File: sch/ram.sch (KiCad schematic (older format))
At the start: 49 parts

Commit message: Start to move to a bit more affordable components
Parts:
- R24, R39, R40, R41, R42, R43, R44, R45, R46, R7, R77, R78, R79, R8, R80, R9: value 51 -> RES
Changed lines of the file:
@@
 EESchema Schematic File Version 2
+LIBS:aleste-rescue
 LIBS:mylib
 LIBS:power
@@
 encoding utf-8
 Sheet 2 7
-Title "Aleste 520EX"
+Title "Aleste 520M"
 Date "1994-01-04"
 Rev ""
-Comp "Patisonic"
-Comment1 "Restored by Alexander Molodtsov"
-Comment2 "Aleste 520EX"
+Comp "Alexander Molodtsov"
+Comment1 ""
+Comment2 ""
 Comment3 ""
 Comment4 ""
@@
 P 10300 1600
 F 0 "R39" H 10300 1700 50  0000 C CNN
-F 1 "51" H 10300 1500 50  0000 C CNN
+F 1 "RES" H 10300 1500 50  0000 C CNN
 F 2 "MyLib:Resistor_Horizontal_RM7.5mm" H 10300 1550 60  0001 C CNN
 F 3 "" H 10300 1550 60  0000 C CNN
@@
 P 10300 2500
 F 0 "R40" H 10300 2600 50  0000 C CNN
-F 1 "51" H 10300 2400 50  0000 C CNN
+F 1 "RES" H 10300 2400 50  0000 C CNN
 F 2 "MyLib:Resistor_Horizontal_RM7.5mm" H 10300 2450 60  0001 C CNN
 F 3 "" H 10300 2450 60  0000 C CNN
@@
 P 10300 3500
 F 0 "R41" H 10300 3600 50  0000 C CNN
-F 1 "51" H 10300 3400 50  0000 C CNN
+F 1 "RES" H 10300 3400 50  0000 C CNN
 F 2 "MyLib:Resistor_Horizontal_RM7.5mm" H 10300 3450 60  0001 C CNN
 F 3 "" H 10300 3450 60  0000 C CNN
@@
 P 10300 4400
 F 0 "R42" H 10300 4500 50  0000 C CNN
-F 1 "51" H 10300 4300 50  0000 C CNN
+F 1 "RES" H 10300 4300 50  0000 C CNN
 F 2 "MyLib:Resistor_Horizontal_RM7.5mm" H 10300 4350 60  0001 C CNN
 F 3 "" H 10300 4350 60  0000 C CNN
@@
 P 10300 5400
 F 0 "R43" H 10300 5500 50  0000 C CNN
-F 1 "51" H 10300 5300 50  0000 C CNN
+F 1 "RES" H 10300 5300 50  0000 C CNN
 F 2 "MyLib:Resistor_Horizontal_RM7.5mm" H 10300 5350 60  0001 C CNN
 F 3 "" H 10300 5350 60  0000 C CNN
@@
 P 10300 6300
 F 0 "R44" H 10300 6400 50  0000 C CNN
-F 1 "51" H 10300 6200 50  0000 C CNN
+F 1 "RES" H 10300 6200 50  0000 C CNN
 F 2 "MyLib:Resistor_Horizontal_RM7.5mm" H 10300 6250 60  0001 C CNN
 F 3 "" H 10300 6250 60  0000 C CNN
@@
 P 10300 7300
 F 0 "R45" H 10300 7400 50  0000 C CNN
-F 1 "51" H 10300 7200 50  0000 C CNN
+F 1 "RES" H 10300 7200 50  0000 C CNN
 F 2 "MyLib:Resistor_Horizontal_RM7.5mm" H 10300 7250 60  0001 C CNN
 F 3 "" H 10300 7250 60  0000 C CNN
@@
 P 10300 8200
 F 0 "R46" H 10300 8300 50  0000 C CNN
-F 1 "51" H 10300 8100 50  0000 C CNN
+F 1 "RES" H 10300 8100 50  0000 C CNN
 F 2 "MyLib:Resistor_Horizontal_RM7.5mm" H 10300 8150 60  0001 C CNN
 F 3 "" H 10300 8150 60  0000 C CNN
@@
 P 10300 9000
 F 0 "R24" H 10300 9100 50  0000 C CNN
-F 1 "51" H 10300 8900 50  0000 C CNN
+F 1 "RES" H 10300 8900 50  0000 C CNN
 F 2 "MyLib:Resistor_Horizontal_RM7.5mm" H 10300 8950 60  0001 C CNN
 F 3 "" H 10300 8950 60  0000 C CNN
@@
 P 3100 9700
 F 0 "R7" H 3100 9800 50  0000 C CNN
-F 1 "51" H 3100 9600 50  0000 C CNN
+F 1 "RES" H 3100 9600 50  0000 C CNN
 F 2 "MyLib:Resistor_Horizontal_RM7.5mm" H 3100 9650 60  0001 C CNN
 F 3 "" H 3100 9650 60  0000 C CNN
@@
 P 3500 10400
 F 0 "R9" H 3500 10500 50  0000 C CNN
-F 1 "51" H 3500 10300 50  0000 C CNN
+F 1 "RES" H 3500 10300 50  0000 C CNN
 F 2 "MyLib:Resistor_Horizontal_RM7.5mm" H 3500 10350 60  0001 C CNN
 F 3 "" H 3500 10350 60  0000 C CNN
@@
 P 3500 10900
 F 0 "R8" H 3500 11000 50  0000 C CNN
-F 1 "51" H 3500 10800 50  0000 C CNN
+F 1 "RES" H 3500 10800 50  0000 C CNN
 F 2 "MyLib:Resistor_Horizontal_RM7.5mm" H 3500 10850 60  0001 C CNN
 F 3 "" H 3500 10850 60  0000 C CNN
@@
 P 3000 13800
 F 0 "R77" H 3000 13900 50  0000 C CNN
-F 1 "51" H 3000 13700 50  0000 C CNN
+F 1 "RES" H 3000 13700 50  0000 C CNN
 F 2 "MyLib:Resistor_Horizontal_RM7.5mm" H 3000 13750 60  0001 C CNN
 F 3 "" H 3000 13750 60  0000 C CNN
@@
 P 3400 14000
 F 0 "R78" H 3400 14100 50  0000 C CNN
-F 1 "51" H 3400 13900 50  0000 C CNN
+F 1 "RES" H 3400 13900 50  0000 C CNN
 F 2 "MyLib:Resistor_Horizontal_RM7.5mm" H 3400 13950 60  0001 C CNN
 F 3 "" H 3400 13950 60  0000 C CNN
@@
 P 3000 14200
 F 0 "R79" H 3000 14300 50  0000 C CNN
-F 1 "51" H 3000 14100 50  0000 C CNN
+F 1 "RES" H 3000 14100 50  0000 C CNN
 F 2 "MyLib:Resistor_Horizontal_RM7.5mm" H 3000 14150 60  0001 C CNN
 F 3 "" H 3000 14150 60  0000 C CNN
@@
 P 3400 14400
 F 0 "R80" H 3400 14500 50  0000 C CNN
-F 1 "51" H 3400 14300 50  0000 C CNN
+F 1 "RES" H 3400 14300 50  0000 C CNN
 F 2 "MyLib:Resistor_Horizontal_RM7.5mm" H 3400 14350 60  0001 C CNN
 F 3 "" H 3400 14350 60  0000 C CNN

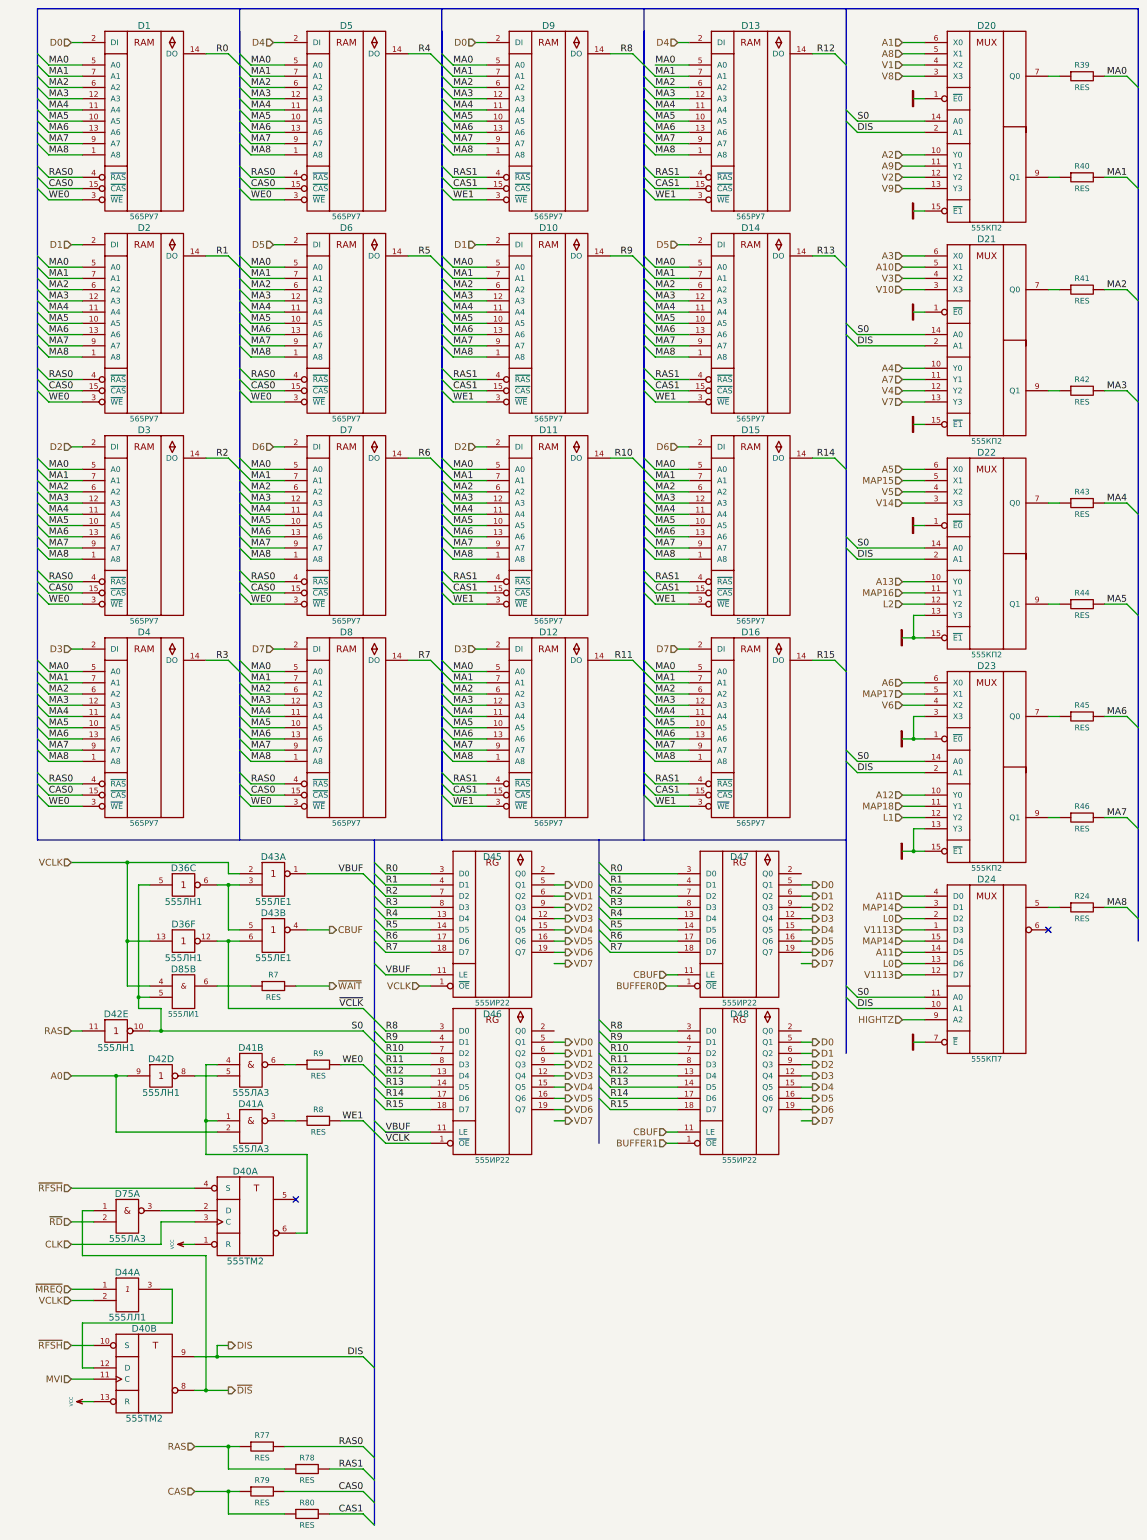
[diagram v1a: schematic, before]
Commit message: Update IR22 and IR23 symbols
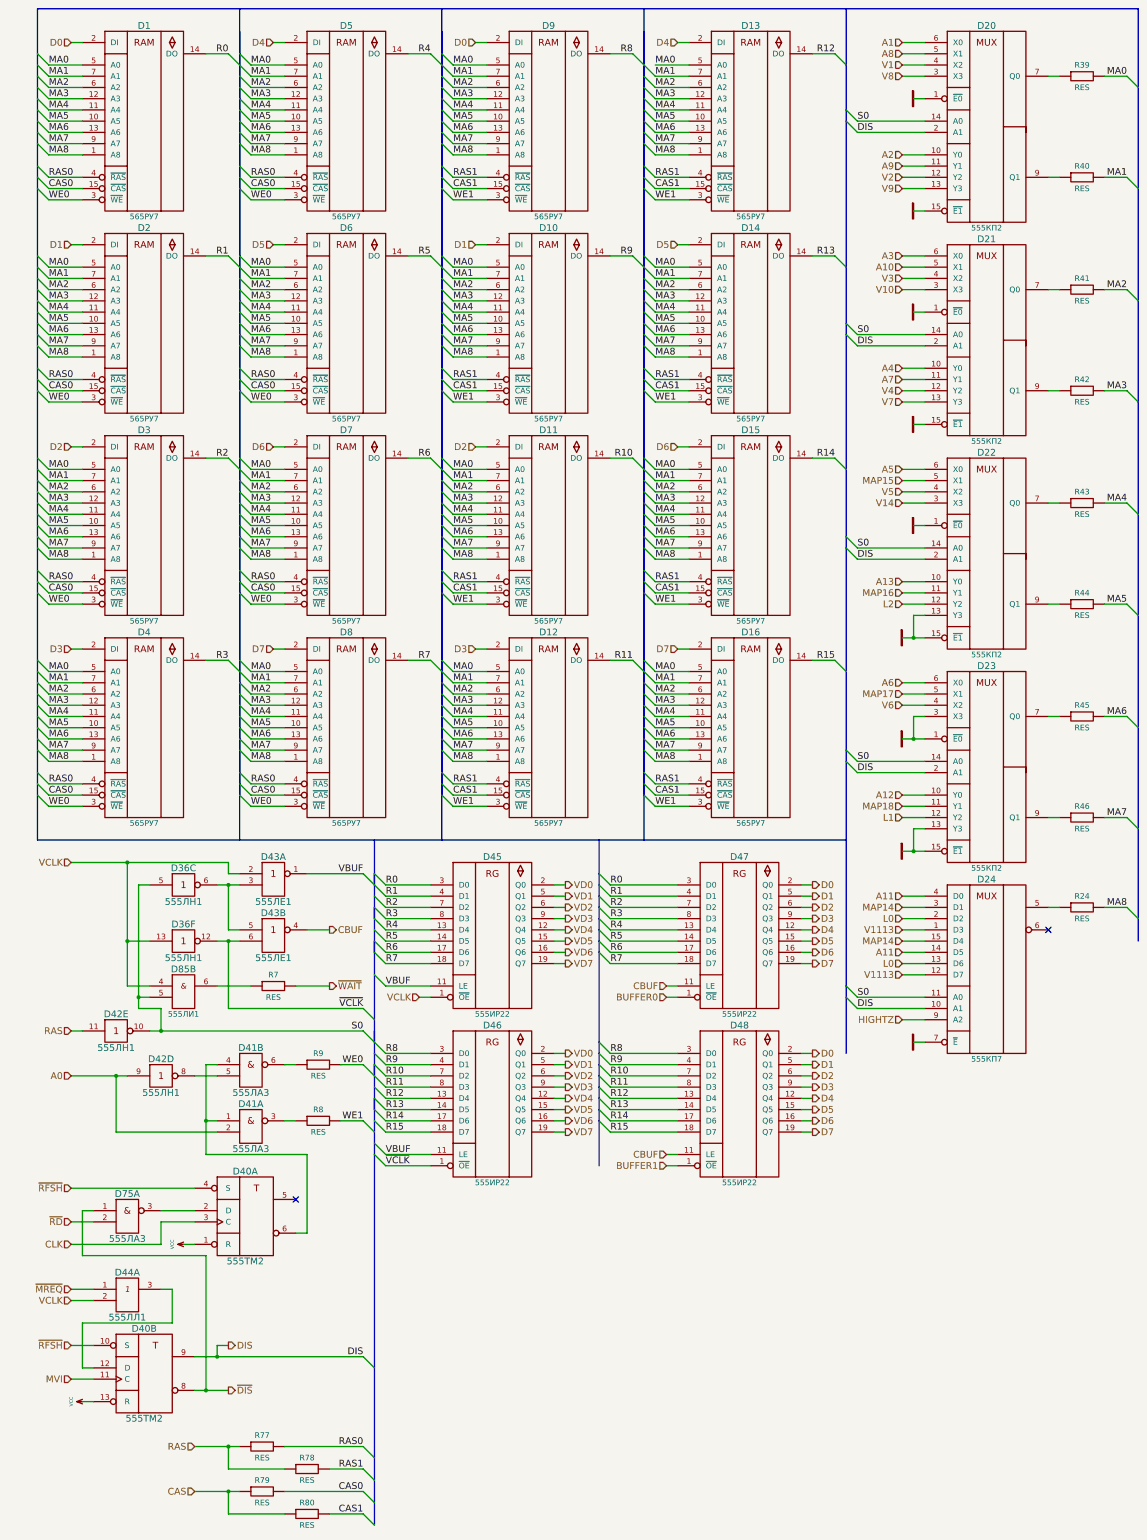
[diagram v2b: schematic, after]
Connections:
- net D0: now also D47.2 (Q0), D48.2 (Q0); no longer D47.5 (Q1), D48.5 (Q1)
- net D1: now also D47.5 (Q1), D48.5 (Q1); no longer D47.6 (Q2), D48.6 (Q2)
- net D2: now also D47.6 (Q2), D48.6 (Q2); no longer D47.9 (Q3), D48.9 (Q3)
- net D3: now also D47.9 (Q3), D48.9 (Q3); no longer D47.12 (Q4), D48.12 (Q4)
- net D4: now also D47.12 (Q4), D48.12 (Q4); no longer D47.15 (Q5), D48.15 (Q5)
- net D5: now also D47.15 (Q5), D48.15 (Q5); no longer D47.16 (Q6), D48.16 (Q6)
- net D6: now also D47.16 (Q6), D48.16 (Q6); no longer D47.19 (Q7), D48.19 (Q7)
- net D7: now also D47.19 (Q7), D48.19 (Q7)
- net VD0: now also D45.2 (Q0), D46.2 (Q0); no longer D45.5 (Q1), D46.5 (Q1)
- net VD1: now also D45.5 (Q1), D46.5 (Q1); no longer D45.6 (Q2), D46.6 (Q2)
- net VD2: now also D45.6 (Q2), D46.6 (Q2); no longer D45.9 (Q3), D46.9 (Q3)
- net VD3: now also D45.9 (Q3), D46.9 (Q3); no longer D45.12 (Q4), D46.12 (Q4)
- net VD4: now also D45.12 (Q4), D46.12 (Q4); no longer D45.15 (Q5), D46.15 (Q5)
- net VD5: now also D45.15 (Q5), D46.15 (Q5); no longer D45.16 (Q6), D46.16 (Q6)
- net VD6: now also D45.16 (Q6), D46.16 (Q6); no longer D45.19 (Q7), D46.19 (Q7)
- net VD7: now also D45.19 (Q7), D46.19 (Q7)
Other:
- moved on the sheet: D45, D46, D47, D48

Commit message: Another ROM replaced with PLD, source included
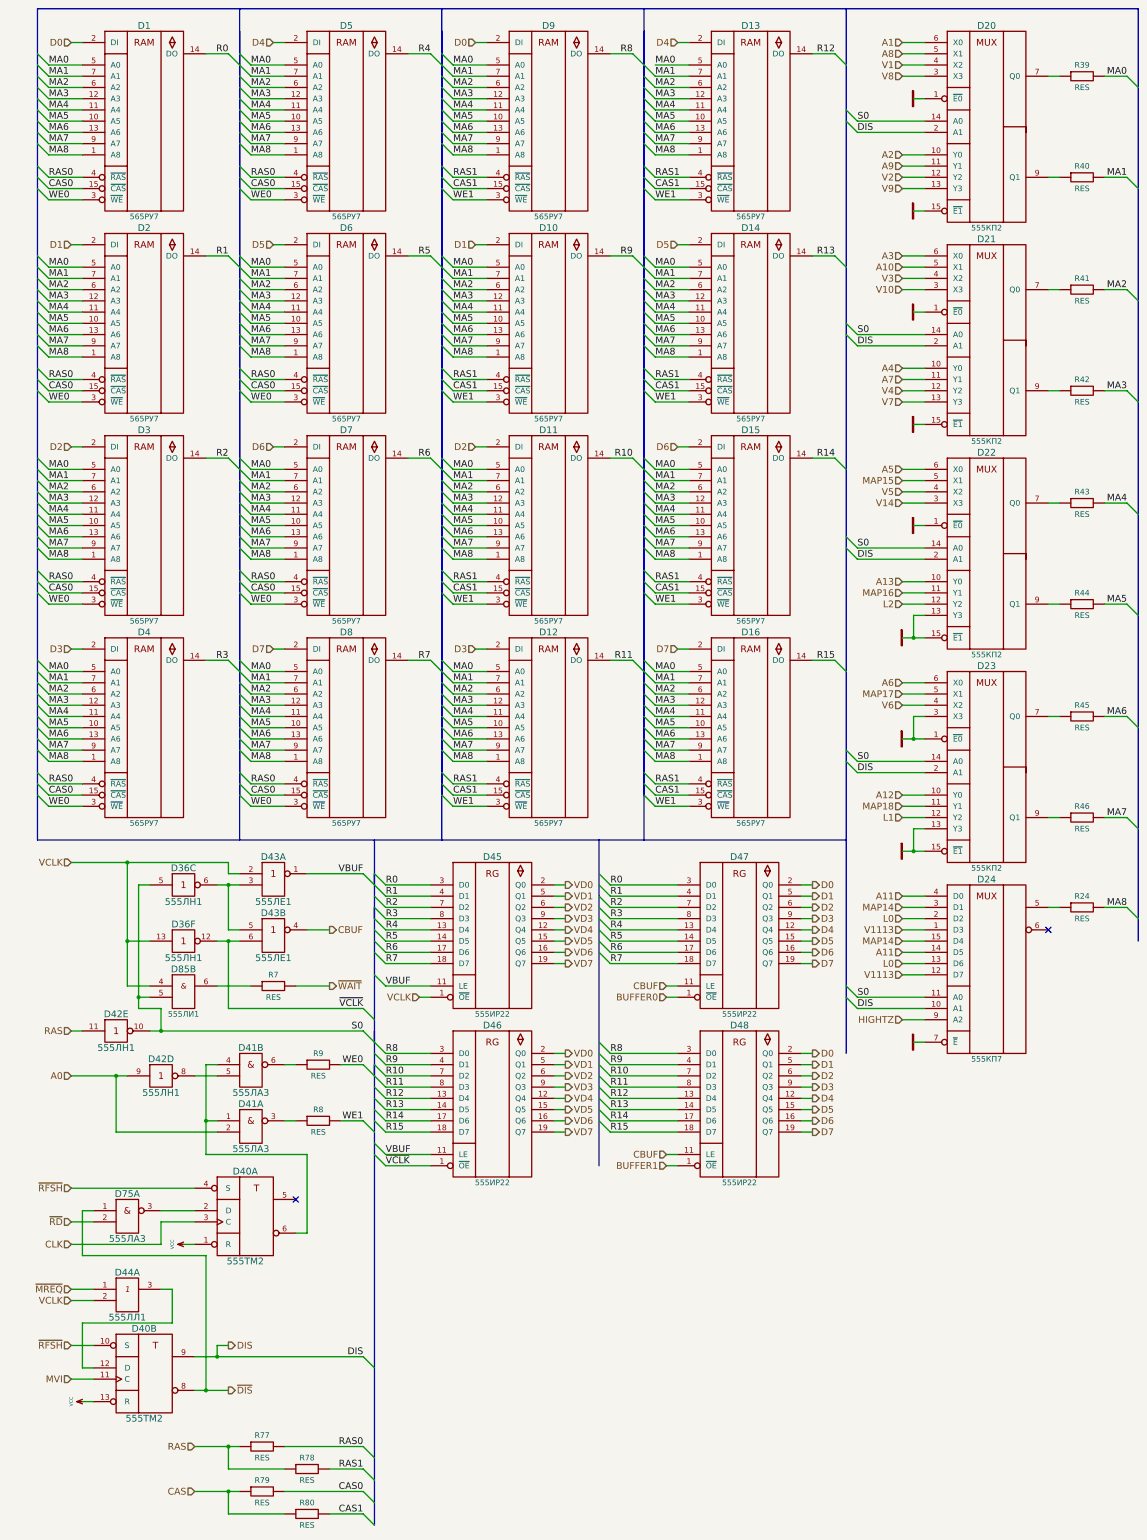
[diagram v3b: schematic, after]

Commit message: Fix MVI signal
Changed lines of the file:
@@
 	2800 8700 2700 8700
 Wire Wire Line
-	2700 8600 2700 8700
+	2700 8700 2700 8600
 Wire Wire Line
-	1300 8600 2700 8600
+	2700 8600 1300 8600
 Connection ~ 1800 9300
 Text HLabel 1300 8600 0    60   Input ~ 0
